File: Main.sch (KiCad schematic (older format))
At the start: 42 parts

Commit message: added new timer circuit and changed deployment switch architecture
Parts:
- removed C?: 0.01uF, symbol Main-rescue:0.01uF-555_timer-rescue
- removed C?: 180uF, symbol Main-rescue:180uF-555_timer-rescue
- removed D? (x4): FET(reversed), symbol Main-rescue:FET(reversed)-555_timer-rescue
- removed D?: Diode, symbol Main-rescue:Diode-555_timer-rescue
- removed R? (x2): 10k, symbol Main-rescue:10k-555_timer-rescue
- removed R?: 10M, symbol Main-rescue:10M-555_timer-rescue
- removed U?: LM555_TIMER, symbol Main-rescue:LM555_TIMER-555_timer-rescue
- added C?: 150u, symbol Device:C
- added C?: 0.1u, symbol Device:C
- added R?: 1M, symbol Device:R
- added R?: 887k, symbol Device:R
- added R?: 86.6k, symbol Device:R
- added R?: R, symbol Device:R
- added SW? (x3): SW_Push, symbol Switch:SW_Push
- added U?: LTC6995-1, symbol CustomSymbols:LTC6995-1
- added U?: TPS2557, symbol Main-rescue:TPS2557-CustomSymbols
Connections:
- net labels removed: Coin_cell, GNDA, SS_EN, Trig
- wire segments 177 -> 166
- no-connect marks 12 -> 14
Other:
- note added: "86.6k resistor sets timer length to 31 minutes.\nLow tolerance required."
- note added: "Deployment Switch"
- note removed: "30 Minute Timer"
- note removed: "System Switch"
- moved on the sheet: C?, R?, U?

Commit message: test commit
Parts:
- removed R?: 250k, symbol Device:R_Shunt
- removed R?: 250k, symbol Device:R
- removed R?: 165k, symbol Device:R_Shunt
- removed R?: 165k, symbol Device:R
- removed U?: MSP430F5529IPN, PN80, symbol Main-rescue:MSP430F5529IPN-MSP430
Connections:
- net labels removed: 3.3V_ADC, 5V_ADC, EPS+, EPS-, Ibat+, Ibat-
- wire segments 166 -> 120
- no-connect marks 14 -> 12

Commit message: first commit
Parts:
- removed C? (x4): 0.1u, symbol Device:C
- removed C? (x4): 150u, symbol Device:C
- removed D?: Diode, symbol 555timer:Diode
- removed J?: USB_A MALE, symbol Connector_Generic:Conn_01x02
- removed J?: USB_A FEMALE, symbol Connector:USB_A
- removed PS?: HS-40012, Converter_ACDC:Converter_ACDC_Hahn_HS-400xx_THT, symbol Converter_ACDC:HS-40012
- removed R? (x4): R, symbol Device:R
- removed R? (x5): TBD, symbol Device:R_Shunt
- removed SW? (x2): SW_Push, symbol Switch:SW_Push
- removed TH?: 10k, symbol Device:Thermistor_NTC
- removed U? (x4): TPS2557, symbol Main-rescue:TPS2557-CustomSymbols
- added BT?: Cell1, symbol Device:Battery_Cell
- added C? (x2): 0.1u, symbol Device:C
- added C?: 22u, symbol Device:C
- added C?: 0.47u, symbol Device:C
- added C?: 10u, symbol Device:C
- added D?: D_Schottky, symbol Device:D_Schottky
- added D? (x2): LED, symbol Device:LED
- added L?: 1.64u, symbol Device:L
- added Q?: Q_PMOS_SDG, symbol Device:Q_PMOS_SDG
- added Q? (x2): CSD17307Q5A, Package_TO_SOT_SMD:TDSON-8-1, symbol Transistor_FET:CSD17307Q5A
- added R?: 330, symbol Device:R
- added R? (x2): 2.2k, symbol Device:R
- added R? (x2): 5M, symbol Device:R
- added R?: 59m, symbol Device:R
- added R? (x2): 2k, symbol Device:R
- added SW? (x2): SW_Push, symbol Switch:SW_Push
- added TP? (x2): TestPoint, symbol Connector:TestPoint
- added U?: BQ297xy, Package_SON:WSON-6_1.5x1.5mm_P0.5mm, symbol Battery_Management:BQ297xy
- added U?: LTC4002ES8-4.2, Package_SO:SOIC-8_3.9x4.9mm_P1.27mm, symbol Battery_Management:LTC4002ES8-4.2
- added U?: TPS2557, symbol Main-rescue:TPS2557-CustomSymbols
- R?: value R -> 20k
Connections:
- net labels added: BAT
- net labels removed: +3.3V, ACS, ACS+, ACS-, Ipv+, Ipv-, OBC, OBC+, OBC-, PAYLOAD, PAYLOAD+, PAYLOAD-, RF, RF+, RF-
- wire segments 120 -> 94
- no-connect marks 12 -> 3
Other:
- note added: "59 mOhms sets Ibat=1.7A"
- note added: "Changes timer duration"
- note added: "Close switch to induce external short"
- note added: "Connect battery to charger"
- note added: "Fake Deployment Switch used to test timer"
- note added: "Must be able to connect DC voltage source to act as battery"
- note added: "Must be able to swap out these 3 resistors"
- note added: "Not sure about this resistor\nLED indicates charging"
- note added: "Not sure what resistor we need to limit LED current\nLED indicates timer up"
- note added: "Overcurrent triggers at 4A"
- note added: "Rds_on = 11 milliOhm each"
- note added: "Replace L to examine affect on ripple current"
- note removed: "86.6k resistor sets timer length to 31 minutes.\nLow tolerance required."
- note removed: "Deployment Switch"
- note removed: "External Charger"
- note removed: "External Charging Circuit\n"
- note removed: "Thermistor"
- moved on the sheet: C?, R?, SW?, U?

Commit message: started assigning footprints
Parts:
- U3: renamed from U?; footprint (none) -> Package_SON:VSON-8_3.3x3.3mm_P0.65mm_NexFET; symbol CustomSymbols:LTC6995-1 -> Main-rescue:LTC6995-1-CustomSymbols
- U4, U5: renamed from U?; footprint (none) -> Package_SON:VSON-8_3.3x3.3mm_P0.65mm_NexFET
- gave numbers to parts that had none: 34

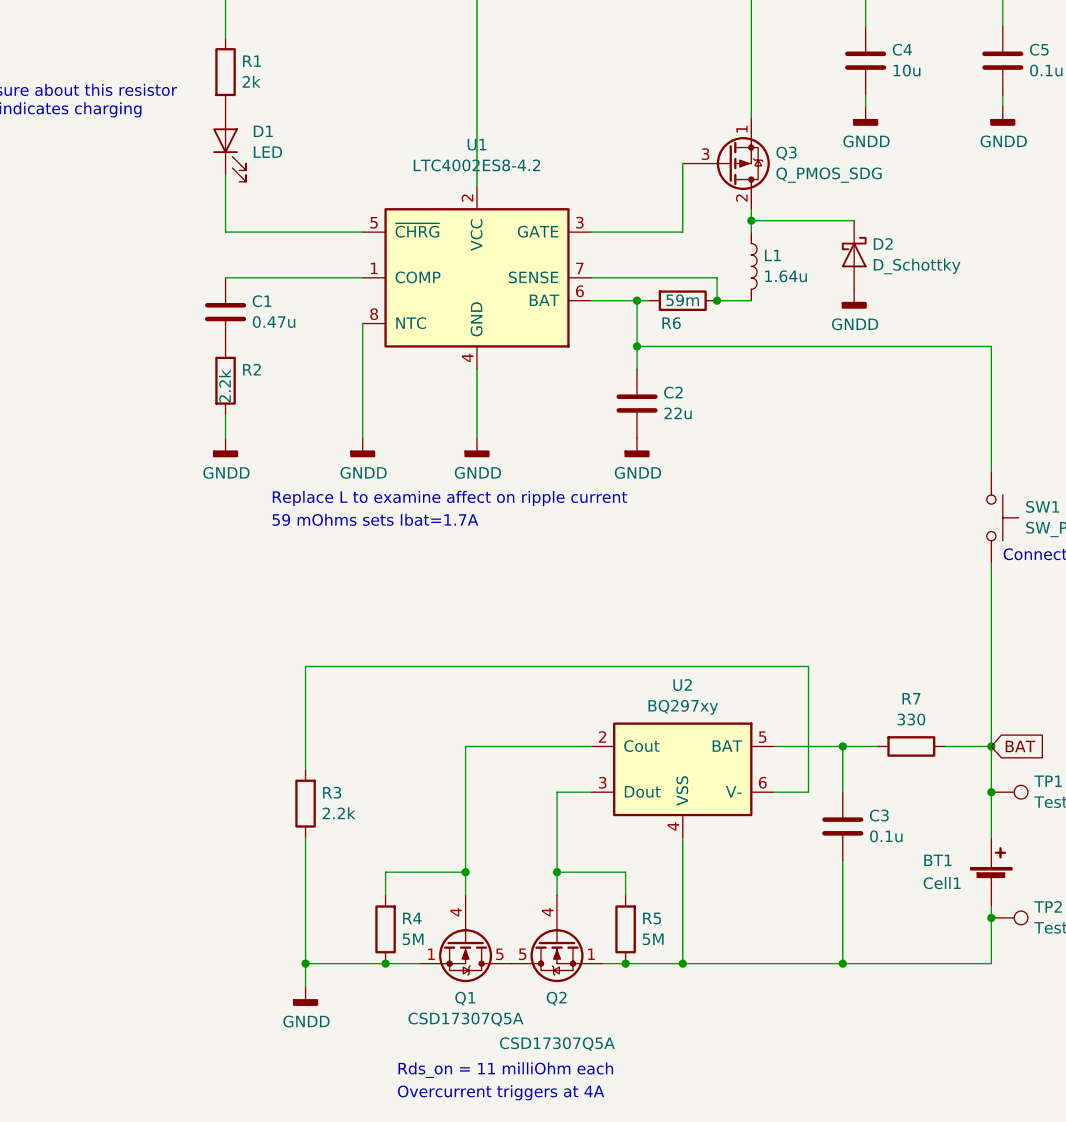
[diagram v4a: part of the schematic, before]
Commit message: added more footprints
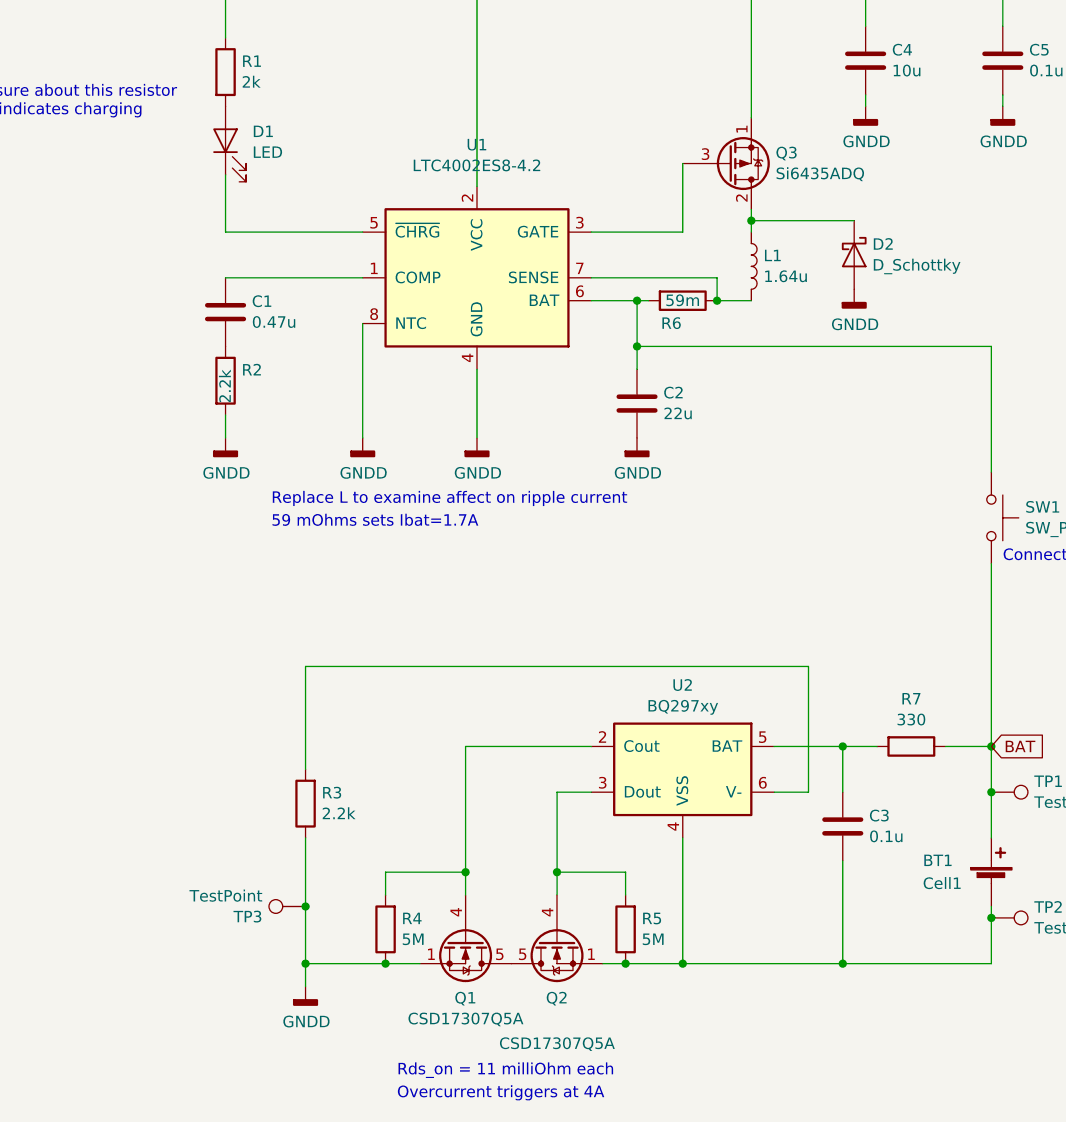
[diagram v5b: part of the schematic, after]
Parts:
- added TP3: TestPoint, Connector_PinHeader_2.00mm:PinHeader_1x01_P2.00mm_Vertical, symbol Connector:TestPoint
- Q3: value Q_PMOS_SDG -> Si6435ADQ; footprint (none) -> Package_SO:TSSOP-8_4.4x3mm_P0.65mm
- TP1, TP2: footprint (none) -> Connector_PinHeader_2.00mm:PinHeader_1x01_P2.00mm_Vertical
- U3: footprint Package_SON:VSON-8_3.3x3.3mm_P0.65mm_NexFET -> Package_TO_SOT_SMD:TSOT-23-6
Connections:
- net GNDD: now also TP3.1
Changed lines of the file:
@@
 F 0 "U3" H 9525 6165 50  0000 C CNN
 F 1 "LTC6995-1" H 9525 6074 50  0000 C CNN
-F 2 "Package_SON:VSON-8_3.3x3.3mm_P0.65mm_NexFET" H 9550 5650 50  0001 C CNN
+F 2 "Package_TO_SOT_SMD:TSOT-23-6" H 9550 5650 50  0001 C CNN
 F 3 "" H 9550 5650 50  0001 C CNN
 	1    9550 5650
@@
 	4600 7650 4600 8200
 Wire Wire Line
-	3900 8050 3900 8600
+	3900 8050 3900 8350
 $Comp
 L Device:R R4
@@
 P 5750 5100
 F 0 "Q3" H 5956 5054 50  0000 L CNN
-F 1 "Q_PMOS_SDG" H 5956 5145 50  0000 L CNN
-F 2 "" H 5950 5200 50  0001 C CNN
+F 1 "Si6435ADQ" H 5956 5145 50  0000 L CNN
+F 2 "Package_SO:TSSOP-8_4.4x3mm_P0.65mm" H 5950 5200 50  0001 C CNN
 F 3 "~" H 5750 5100 50  0001 C CNN
 	1    5750 5100
@@
 F 0 "TP1" V 6854 8038 50  0000 L CNN
 F 1 "TestPoint" V 6945 8038 50  0000 L CNN
-F 2 "" H 7100 7850 50  0001 C CNN
+F 2 "Connector_PinHeader_2.00mm:PinHeader_1x01_P2.00mm_Vertical" H 7100 7850 50  0001 C CNN
 F 3 "~" H 7100 7850 50  0001 C CNN
 	1    6900 7850
@@
 F 0 "TP2" V 6854 8588 50  0000 L CNN
 F 1 "TestPoint" V 6945 8588 50  0000 L CNN
-F 2 "" H 7100 8400 50  0001 C CNN
+F 2 "Connector_PinHeader_2.00mm:PinHeader_1x01_P2.00mm_Vertical" H 7100 8400 50  0001 C CNN
 F 3 "~" H 7100 8400 50  0001 C CNN
 	1    6900 8400
@@
 	0    -1   1    0
 $EndComp
+$Comp
+L Connector:TestPoint TP3
+U 1 1 5D080B5D
+P 3900 8350
+F 0 "TP3" V 3854 8538 50  0000 L CNN
+F 1 "TestPoint" V 3945 8538 50  0000 L CNN
+F 2 "Connector_PinHeader_2.00mm:PinHeader_1x01_P2.00mm_Vertical" H 4100 8350 50  0001 C CNN
+F 3 "~" H 4100 8350 50  0001 C CNN
+	1    3900 8350
+	0    -1   -1   0
+$EndComp
+Connection ~ 3900 8350
+Wire Wire Line
+	3900 8350 3900 8600
 $EndSCHEMATC

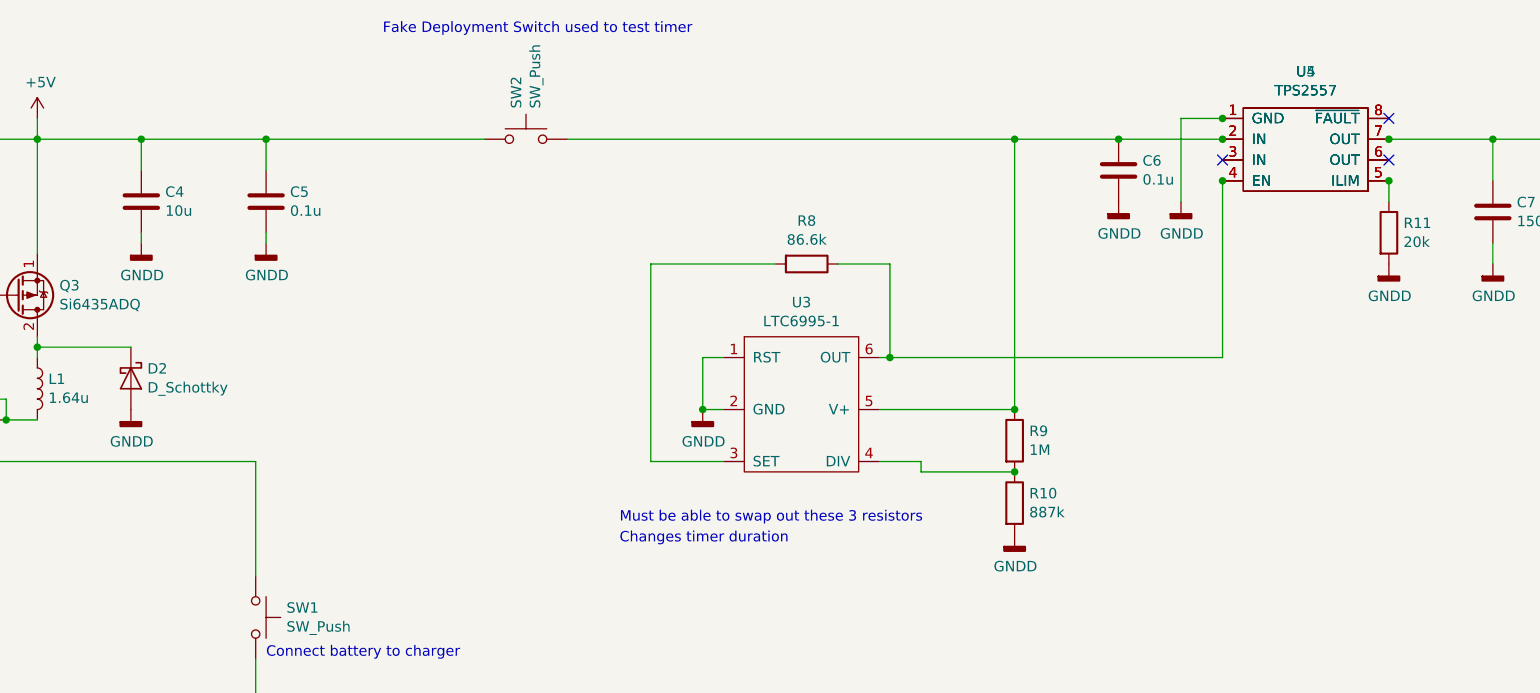
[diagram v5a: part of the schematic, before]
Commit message: need to add tps2557 footprint
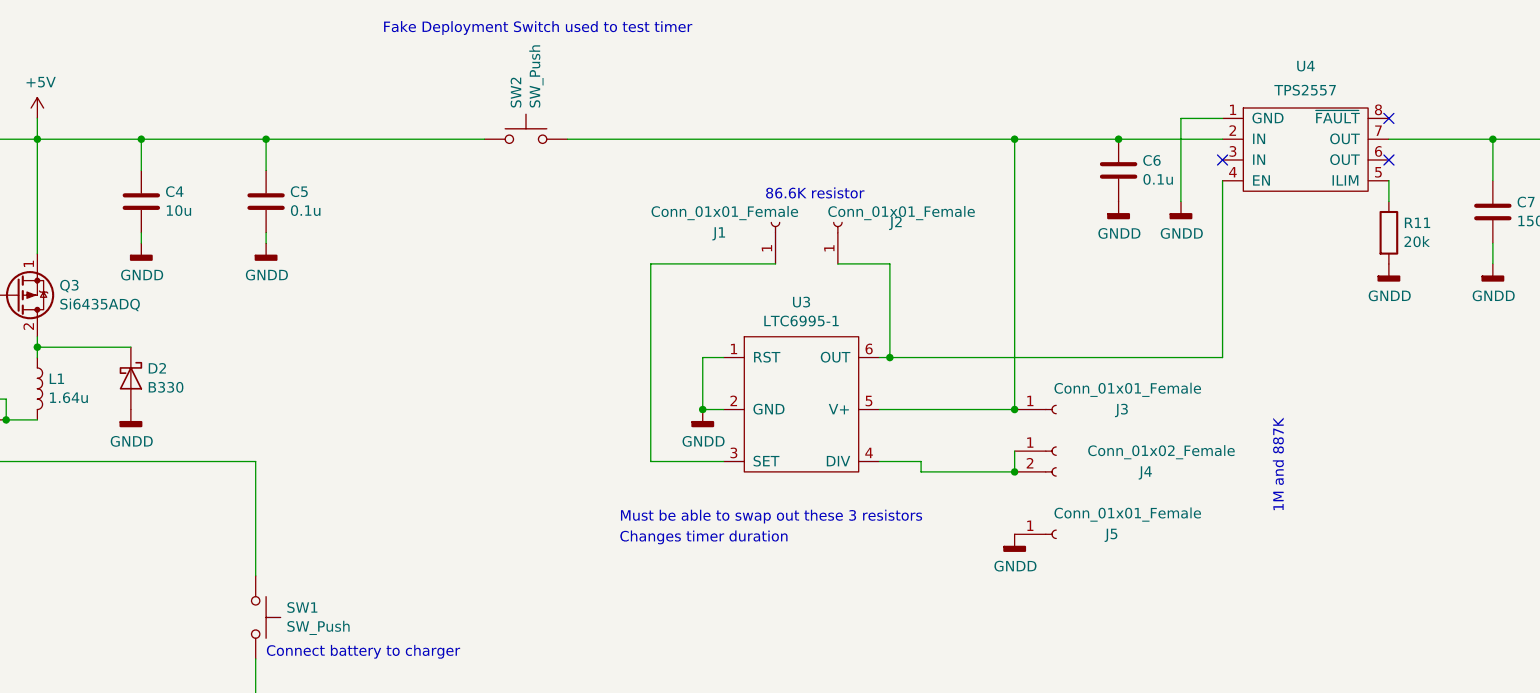
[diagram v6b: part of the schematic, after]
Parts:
- removed D2: D_Schottky, symbol Device:D_Schottky
- removed R10: 887k, symbol Device:R
- removed R8: 86.6k, symbol Device:R
- removed R9: 1M, symbol Device:R
- removed U5: TPS2557, Package_SON:VSON-8_3.3x3.3mm_P0.65mm_NexFET, symbol Main-rescue:TPS2557-CustomSymbols
- added D2: B330, Diode_SMD:D_SMC, symbol Diode:B330
- added J1, J2, J3, J5: Conn_01x01_Female, Connector_PinSocket_2.00mm:PinSocket_1x01_P2.00mm_Vertical, symbol Connector:Conn_01x01_Female
- added J4: Conn_01x02_Female, Connector_PinSocket_2.00mm:PinSocket_1x02_P2.00mm_Vertical, symbol Connector:Conn_01x02_Female
- BT1: footprint (none) -> Battery:BatteryHolder_Keystone_1042_1x18650
- C1, C2, C3, C4, C5, C6, C7: footprint (none) -> Capacitor_SMD:C_1206_3216Metric
- D1, D3: footprint (none) -> LED_SMD:LED_1206_3216Metric
- L1: footprint (none) -> Inductor_SMD:L_1206_3216Metric
- R1, R11, R12, R2, R3, R4, R5, R6, R7: footprint (none) -> Resistor_SMD:R_1206_3216Metric
- SW1, SW2: footprint (none) -> Button_Switch_SMD:SW_DIP_SPSTx01_Slide_6.7x4.1mm_W6.73mm_P2.54mm_LowProfile_JPin
- SW3: footprint (none) -> Button_Switch_SMD:SW_SPST_B3U-1000P
- U4: footprint Package_SON:VSON-8_3.3x3.3mm_P0.65mm_NexFET -> Package_DFN_QFN:DFN-8-1EP_3x3mm_P0.5mm_EP1.66x2.38mm
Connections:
- net GNDD: now also D2.2 (A), J5.1 (Pin_1)
- net at C6.1, SW2.2, U3.5 (V+)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: now also J3.1 (Pin_1)
- net at L1.1, Q3.2 (D): now also D2.1 (K)
- net at U3.3 (SET): now also J1.1 (Pin_1)
- net at U3.4 (DIV): now also J4.1 (Pin_1), J4.2 (Pin_2)
- net at U3.6 (OUT), U4.4 (EN): now also J2.1 (Pin_1)
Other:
- note added: "1M and 887K\n"
- note added: "86.6K resistor"

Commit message: started pcb
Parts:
- U4: footprint Package_DFN_QFN:DFN-8-1EP_3x3mm_P0.5mm_EP1.66x2.38mm -> tps2557:TPS2557
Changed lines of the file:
@@
 F 0 "U4" H 11950 4300 50  0000 C CNN
 F 1 "TPS2557" H 11950 4184 50  0000 C CNN
-F 2 "Package_DFN_QFN:DFN-8-1EP_3x3mm_P0.5mm_EP1.66x2.38mm" H 11950 4150 50  0001 C CNN
+F 2 "tps2557:TPS2557" H 11950 4150 50  0001 C CNN
 F 3 "" H 11950 4150 50  0001 C CNN
 	1    11950 4150

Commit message: finished traces
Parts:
- SW3: footprint Button_Switch_SMD:SW_SPST_B3U-1000P -> Button_Switch_SMD:SW_DIP_SPSTx01_Slide_6.7x4.1mm_W6.73mm_P2.54mm_LowProfile_JPin
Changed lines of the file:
@@
 F 0 "SW3" V 11204 8098 50  0000 L CNN
 F 1 "SW_Push" V 11295 8098 50  0000 L CNN
-F 2 "Button_Switch_SMD:SW_SPST_B3U-1000P" H 11250 8150 50  0001 C CNN
+F 2 "Button_Switch_SMD:SW_DIP_SPSTx01_Slide_6.7x4.1mm_W6.73mm_P2.54mm_LowProfile_JPin" H 11250 8150 50  0001 C CNN
 F 3 "~" H 11250 8150 50  0001 C CNN
 	1    11250 7950
